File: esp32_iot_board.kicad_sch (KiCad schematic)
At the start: 0 parts

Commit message: feat: add libraries folder and initial schematic sections
- Added a libraries folder containing custom symbols, footprints, and 3D models.
- Populated the schematic's front page with five key sections:
    - USB-C Connector
    - LiPo Battery Charger
    - Low Dropout Voltage Regulator
    - Power Indicator LED
    - Battery JST Connector
- Created a second schematic page dedicated to ESP32 circuit design.
- Included relevant datasheets for reference.
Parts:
- added C1, C2, C5: 0u1, symbol Device:C
- added C3, C4: 10u, symbol Device:C_Polarized
- added C6: 1u, symbol Device:C
- added F1: 0ZCH0110AF2E, FUSC3226X100N, symbol 0ZCH0110AF2E:0ZCH0110AF2E
- added J1: SS-52400-002, SS-52400-002:BELFUSE_SS-52400-002, symbol SS-52400-002:SS-52400-002
- added J2: B2B-PH-SM4-TB, B2B-PH-SM4-TB:JST_B2B-PH-SM4-TB, symbol B2B-PH-SM4-TB:B2B-PH-SM4-TB
- added LED1, LED4: LTST-C170KRKT, LEDC2012X120N, symbol LTST-C170KRKT:LTST-C170KRKT
- added LED2: LTST-C170GKT, LEDC2012X120N, symbol LTST-C170GKT:LTST-C170GKT
- added LED3: LTST-C170TBKT, LEDC2012X120N, symbol LTST-C170TBKT:LTST-C170TBKT
- added R1, R2: 5k1, symbol Device:R
- added R10, R7, R8, R9: 470, symbol Device:R
- added R3, R4: 10k, symbol Device:R
- added R5: 2k, symbol Device:R
- added R6: R, symbol Device:R
- added U1: MCP73871, Package_DFN_QFN:QFN-20-1EP_4x4mm_P0.5mm_EP2.5x2.5mm, symbol Battery_Management:MCP73871
- added VR1: LM1117MPX-3.3, LM1117MPX-3.3:VREG_LM1117MPX-3.3, symbol LM1117MPX-3.3:LM1117MPX-3.3
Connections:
- new net: R3.1, U1.9 (~{TE})
- new net: R4.1, U1.5 (THERM)
- new net: R6.2, U1.12 (PROG3)
- new net: J1.A5 (CC1), R2.1
- new net: J1.B5 (CC2), R1.1
- new net: LED3.1 (K), R7.2
- new net: R5.2, U1.13 (PROG1)
- new net: LED1.1 (K), R9.2
- new net: LED2.1 (K), R8.2
- new net +3.3V: C4.1, C5.1, LED4.2 (A), VR1.2 (VOUT_2), VR1.4 (VOUT_4)
- new net +5V: C2.1, C3.1, U1.1 (OUT), U1.20 (OUT), VR1.3 (VIN)
- new net +5v_USB: C6.1, F1.2, LED1.2 (A), LED2.2 (A), LED3.2 (A), U1.17 (CE), U1.18 (IN), U1.19 (IN), U1.2 (VPCC), U1.4 (PROG2)
- new net CHARGED: R8.1, U1.8 (STAT1/~{LBO})
- new net CHARGING: R9.1, U1.6 (~{PG})
- new net CHARGING_POWER_GOOD: R7.1, U1.7 (STAT2)
- new net GND: C1.2, C2.2, C3.2, C4.2, C5.2, C6.2, J1.A1 (GNDA1), J1.A12 (GNDA2), J1.B1 (GNDB1), J1.B12 (GNDB2), J1.G1 (GND/SHIELD), J1.G2 (GND/SHIELD), J1.G3 (GND/SHIELD), J1.G4 (GND/SHIELD), J1.S1 (GND/SHIELD), J1.S2 (GND/SHIELD), J1.S3 (GND/SHIELD), J1.S4 (GND/SHIELD), J2.1, R1.2, R10.1, R2.2, R3.2, R4.2, R5.1, R6.1, U1.10 (V_{SS}), U1.11 (V_{SS}), U1.21 (V_{SS}), VR1.1 (GND)
- new net PW_LED: LED4.1 (K), R10.2
- new net USB_D+: J1.A6 (DP1), J1.B6 (DP2)
- new net USB_D-: J1.A7 (DN1), J1.B7 (DN2)
- new net VBAT: J2.2, U1.14 (V_{BAT}), U1.15 (V_{BAT}), U1.16 (V_{BAT_SENSE})
- new net VBUS: C1.1, F1.1, J1.A4 (VBUSA1), J1.A9 (VBUSA2), J1.B4 (VBUSB1), J1.B9 (VBUSB2)
- no-connect marks 0 -> 10
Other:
- added sheet ESP32-C3-02 (esp32-c3-02.kicad_sch)
- note added: "Battery JST Connector"
- note added: "Lipo battery charger"
- note added: "Low dropout voltage regulator"
- note added: "Power indicator LED"
- note added: "USB_C CONNECTOR"

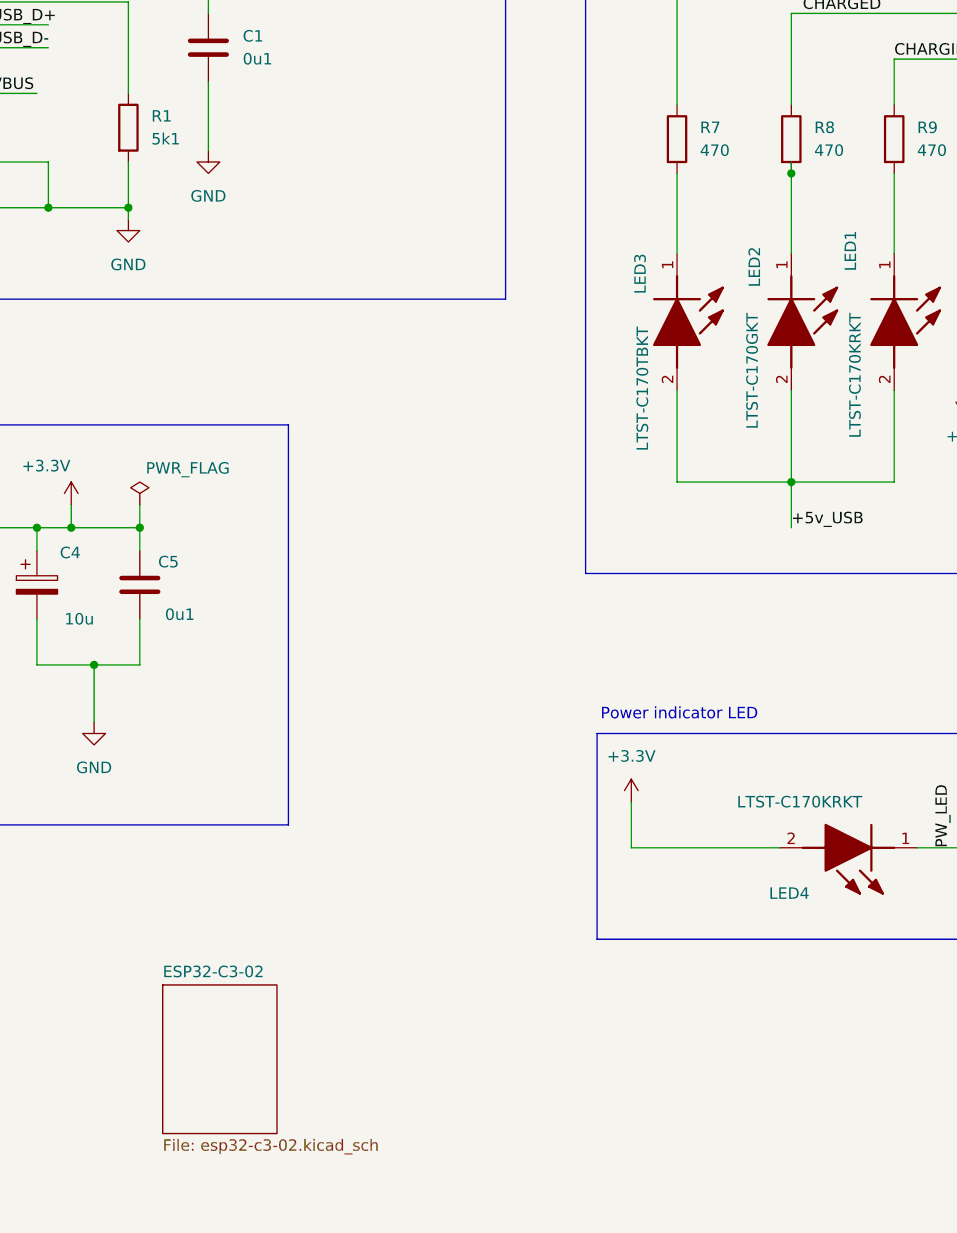
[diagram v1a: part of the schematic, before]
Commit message: feat: add sensor and user interface schematic sheets, update ESP32 sheet
- Added Sensors schematic sheet for integrating all sensor-related components.
- Added User Interface sheet to host user-interaction components (e.g., buttons, displays).
- Populated the ESP32 sheet with the following sections:
    - USB-to-UART Connector
    - ESP32 Module
    - Flash Memory
    - SD Card Module
- Each section is modular and self-contained, designed for clarity and easy testing.
- Enabled signal access (e.g., USB_D+, USB_D-, VBUS) in the USB-to-UART section via hierarchical labels from the parent sheet.
- Added test points on SPI lines within the ESP32 sheet to facilitate hardware debugging and validation.
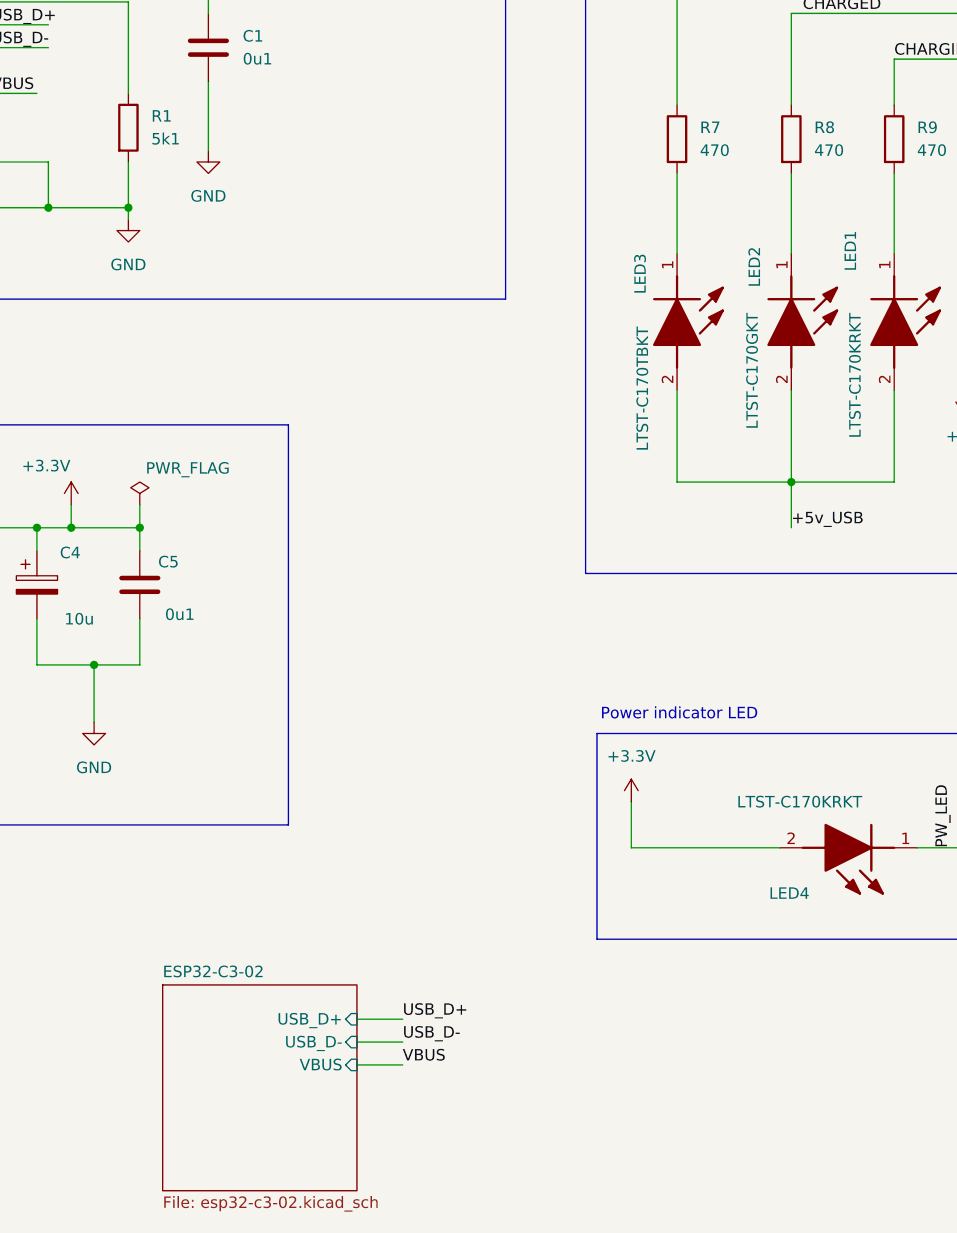
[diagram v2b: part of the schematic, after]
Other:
- sheet ESP32-C3-02 ports: added USB_D+, USB_D-, VBUS; removed none
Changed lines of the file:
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@@
 	)
 	(junction
-		(at 166.37 60.96)
-		(diameter 0)
-		(color 0 0 0 0)
-	)
-	(junction
 		(at 82.55 100.33)
 		(diameter 0)
@@
 	(wire
 		(pts
+			(xy 118.11 157.48) (xy 123.19 157.48)
+		)
+		(stroke
+			(width 0)
+			(type default)
+		)
+	)
+	(wire
+		(pts
 			(xy 177.8 85.09) (xy 177.8 95.25)
 		)
@@
 	(wire
 		(pts
-			(xy 31.75 39.37) (xy 36.83 39.37)
+			(xy 118.11 154.94) (xy 123.19 154.94)
 		)
 		(stroke
@@
 	(wire
 		(pts
-			(xy 30.48 44.45) (xy 36.83 44.45)
+			(xy 31.75 39.37) (xy 36.83 39.37)
 		)
 		(stroke
@@
 	(wire
 		(pts
-			(xy 82.55 115.57) (xy 88.9 115.57)
+			(xy 30.48 44.45) (xy 36.83 44.45)
 		)
 		(stroke
@@
 	(wire
 		(pts
-			(xy 36.83 59.69) (xy 30.48 59.69)
+			(xy 82.55 115.57) (xy 88.9 115.57)
 		)
 		(stroke
@@
 	(wire
 		(pts
-			(xy 166.37 85.09) (xy 166.37 95.25)
+			(xy 36.83 59.69) (xy 30.48 59.69)
 		)
 		(stroke
@@
 	(wire
 		(pts
-			(xy 86.36 100.33) (xy 93.98 100.33)
+			(xy 166.37 85.09) (xy 166.37 95.25)
 		)
 		(stroke
@@
 	(wire
 		(pts
-			(xy 153.67 85.09) (xy 153.67 95.25)
+			(xy 86.36 100.33) (xy 93.98 100.33)
 		)
 		(stroke
@@
 	(wire
 		(pts
-			(xy 83.82 59.69) (xy 83.82 64.77)
+			(xy 153.67 85.09) (xy 153.67 95.25)
 		)
 		(stroke
@@
 	(wire
 		(pts
-			(xy 166.37 59.69) (xy 166.37 60.96)
+			(xy 83.82 59.69) (xy 83.82 64.77)
 		)
 		(stroke
@@
 	(wire
 		(pts
+			(xy 118.11 160.02) (xy 123.19 160.02)
+		)
+		(stroke
+			(width 0)
+			(type default)
+		)
+	)
+	(wire
+		(pts
 			(xy 187.96 55.88) (xy 187.96 60.96)
 		)
@@
 	)
 	(label "USB_D+"
+		(at 123.19 154.94 0)
+		(effects
+			(font
+				(size 1.27 1.27)
+			)
+			(justify left bottom)
+		)
+	)
+	(label "USB_D+"
 		(at 30.48 44.45 0)
 		(effects
@@
 		)
 	)
+	(label "VBUS"
+		(at 123.19 160.02 0)
+		(effects
+			(font
+				(size 1.27 1.27)
+			)
+			(justify left bottom)
+		)
+	)
 	(label "VBAT"
 		(at 187.96 59.69 90)
@@
 		)
 	)
+	(label "USB_D-"
+		(at 123.19 157.48 0)
+		(effects
+			(font
+				(size 1.27 1.27)
+			)
+			(justify left bottom)
+		)
+	)
 	(label "+5v_USB"
 		(at 123.19 39.37 0)
@@
 	(sheet
 		(at 96.52 151.13)
-		(size 12.7 16.51)
+		(size 21.59 22.86)
 		(exclude_from_sim no)
 		(in_bom yes)
@@
 		)
 		(property "Sheetfile" "esp32-c3-02.kicad_sch"
-			(at 96.52 168.2246 0)
+			(at 96.52 174.5746 0)
 			(effects
 				(font
@@
 			)
 		)
+		(pin "USB_D+" input
+			(at 118.11 154.94 0)
+			(effects
+				(font
+					(size 1.27 1.27)
+				)
+				(justify right)
+			)
+		)
+		(pin "USB_D-" input
+			(at 118.11 157.48 0)
+			(effects
+				(font
+					(size 1.27 1.27)
+				)
+				(justify right)
+			)
+		)
+		(pin "VBUS" input
+			(at 118.11 160.02 0)
+			(effects
+				(font
+					(size 1.27 1.27)
+				)
+				(justify right)
+			)
+		)

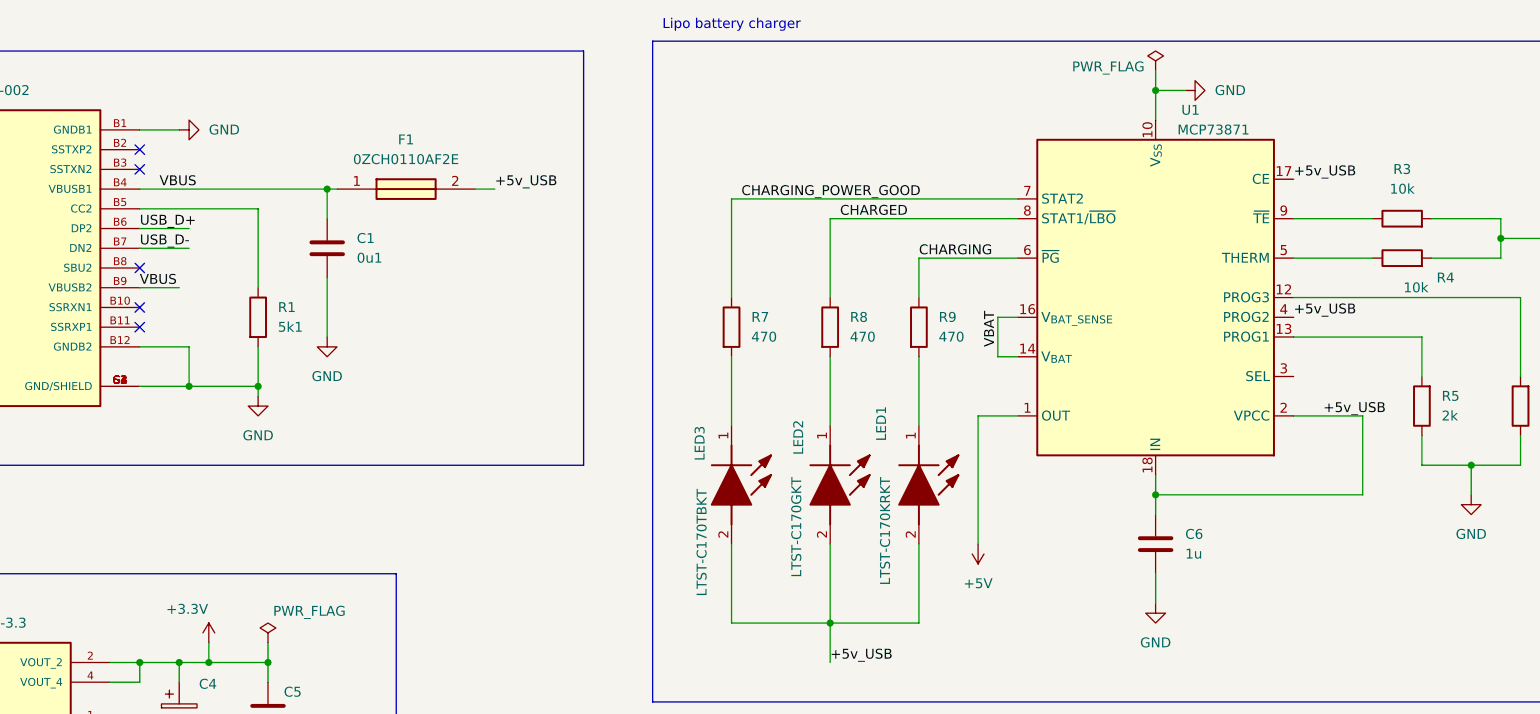
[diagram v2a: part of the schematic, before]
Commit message: feat: populate sensor and user interface schematic sheets; assign footprints
- Populated the Sensors schematic sheet with the following components:
    - BME280: Temperature and humidity sensor
    - Photoresistor: For measuring ambient light levels
    - Sound Sensor Section: Includes a microphone and preamplifier to amplify audio signals for microcontroller processing

- Populated the User Interface schematic sheet with:
    - Boot and reset controls for the microcontroller
    - Breakout lines for external devices:
        - One for I²C-based peripherals (e.g., OLED display)
        - One for general-purpose I/O devices

- Both the Sensors and User Interface sheets access necessary pins (e.g., I²C, GPIO, control signals) from the parent ESP32
sheet using hierarchical labels, enabling clean and modular design.

- Assigned appropriate footprints to all components.
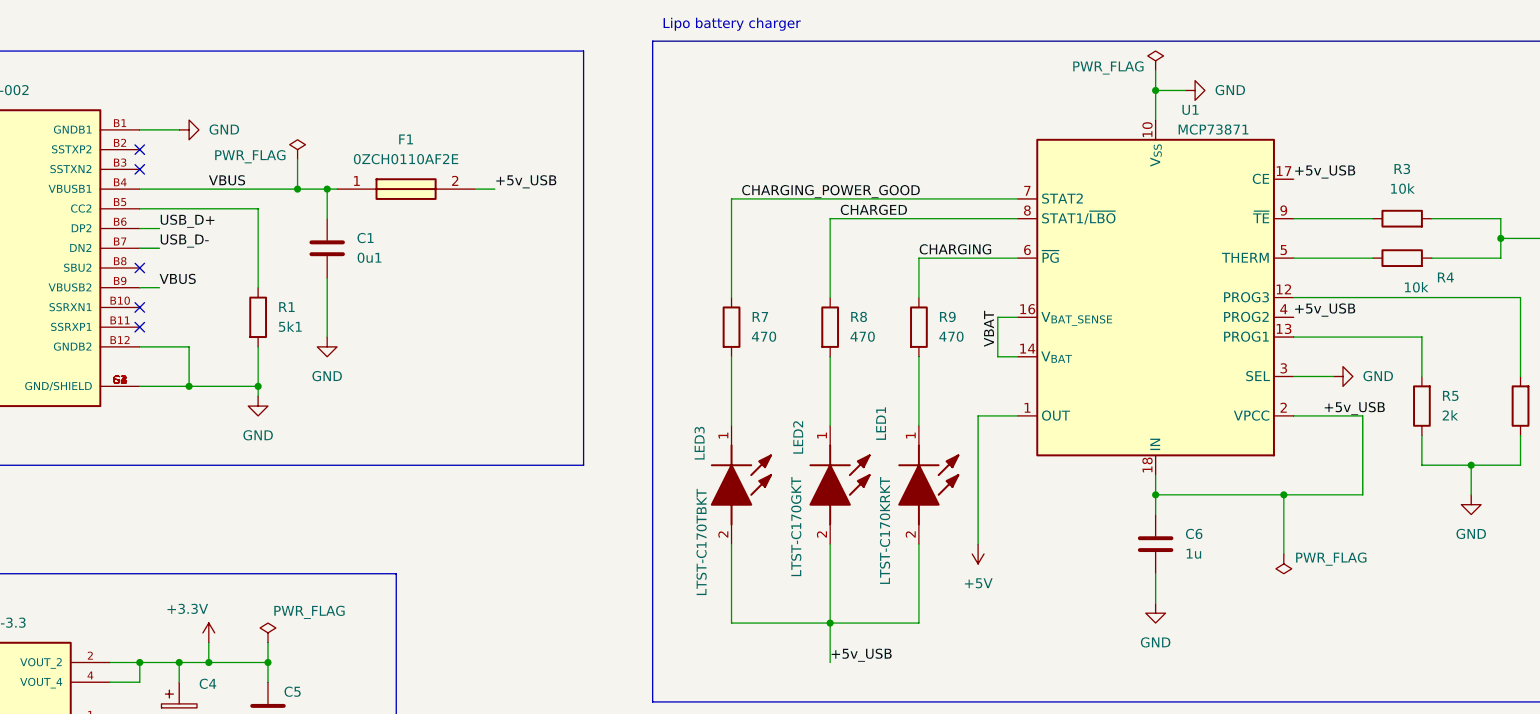
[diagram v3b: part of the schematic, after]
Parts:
- C1, C2, C5, C6: footprint (none) -> Capacitor_SMD:C_0805_2012Metric
- C3, C4: footprint (none) -> ESP32 Project Footprints:T491A
- F1: footprint FUSC3226X100N -> ESP32 Project Footprints:FUSC3226X100N
- LED1, LED2, LED3, LED4: footprint LEDC2012X120N -> ESP32 Project Footprints:LEDC2012X120N
- R1, R10, R2, R3, R4, R5, R6, R7, R8, R9: footprint (none) -> Resistor_SMD:R_0805_2012Metric
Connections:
- net GND: now also U1.3 (SEL)
